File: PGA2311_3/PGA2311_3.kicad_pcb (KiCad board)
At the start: 2 copper layers, 234 x 58 mm, 210 parts, among them J201 3, J202 3, J203 2, J204 2, J205 2, J206 2, J301 Conn_01x16, J302 1, J303 Conn_01x02, J304 4, J305 4, J401 1, J402 3, J403 1, Q301 BC817-40, SW301 SW_Push, SW302 Encoder PEC11R, U201 OPA1678IDR, U202 CD74HCT4052, U203 CD74HCT4052, U204 LM337LM, U205 PGA2311UA, U206 LM317LIDR, U207 UA78L05AIDR, U301 TPS60403DBV, U302 WH1602B, U303 SN74LVC8T245DW, U304 STM32G070KBT6, U305 TLV1117-50IDC, U306 LP2985-33DBV, U307 SN74LVC2G17DBV

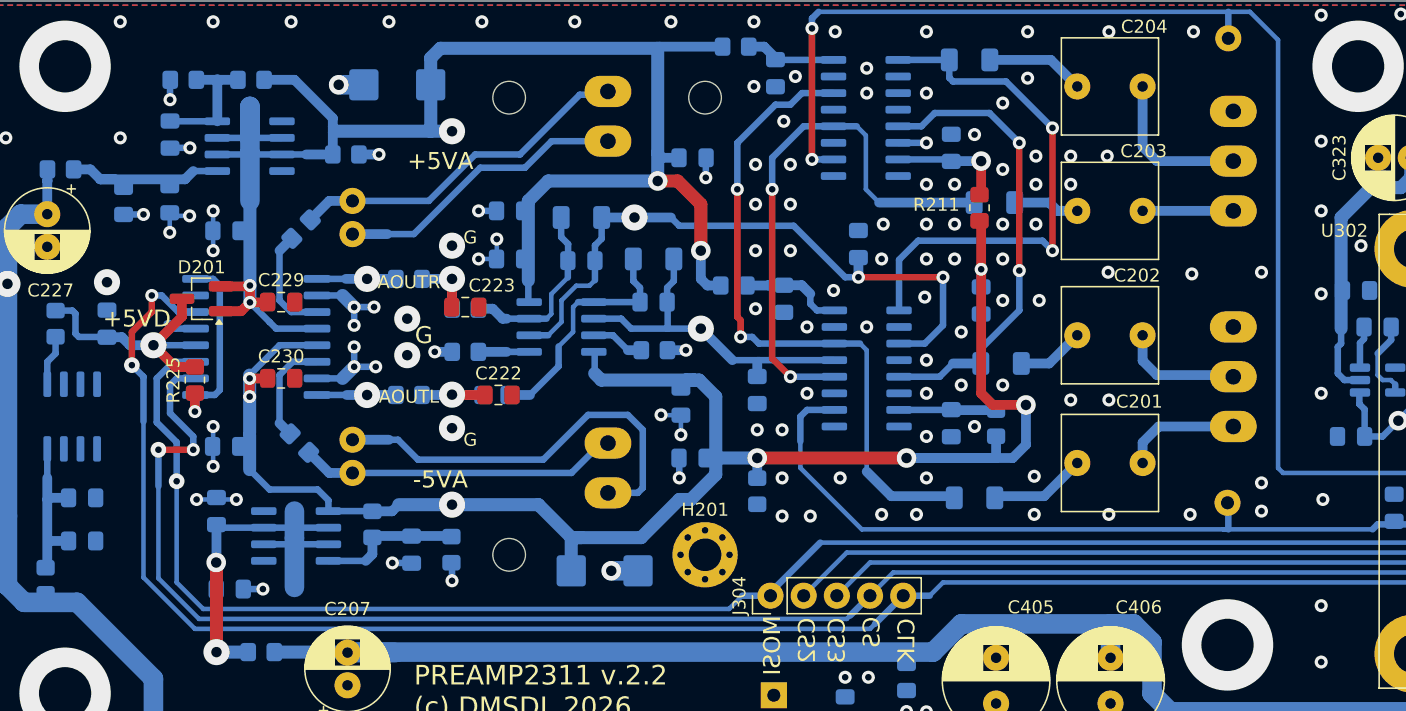
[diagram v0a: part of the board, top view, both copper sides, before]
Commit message: Add files via upload
vias rearranged for connector placement
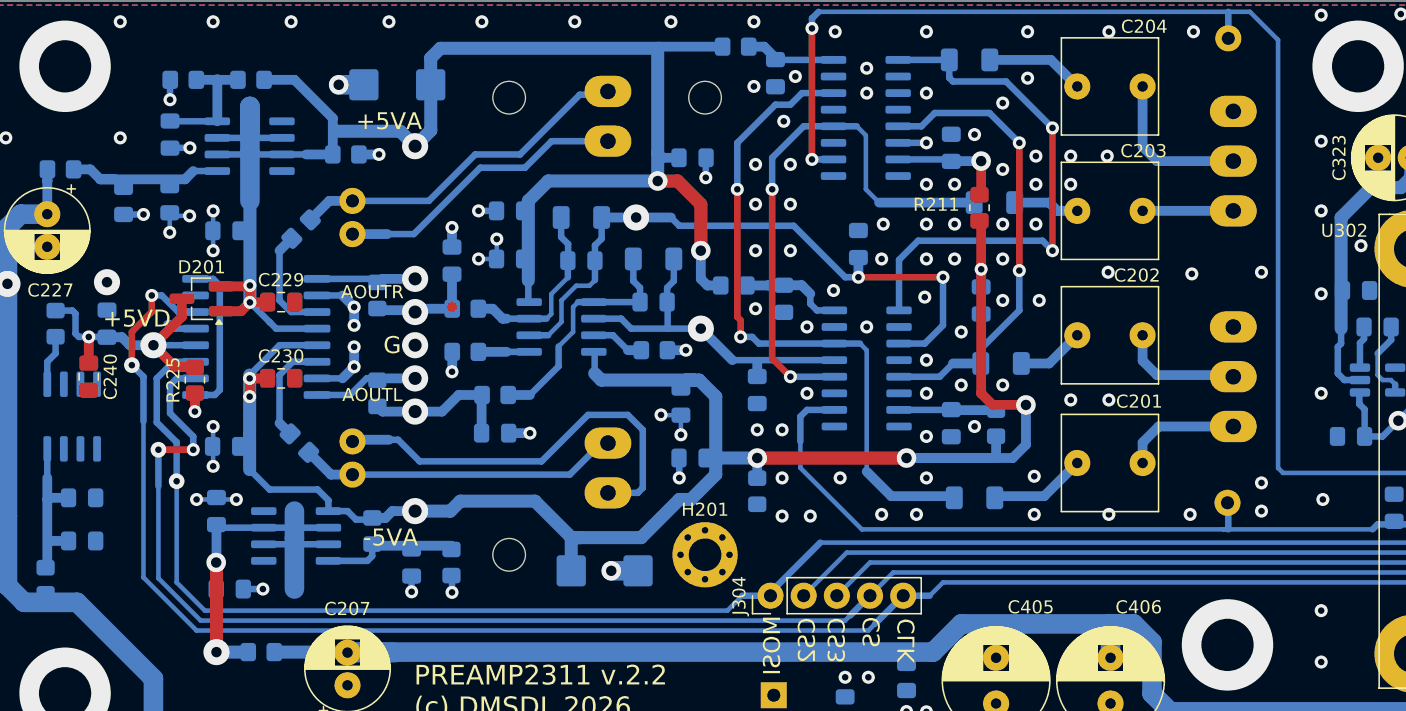
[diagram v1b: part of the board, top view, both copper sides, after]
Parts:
- added C240: 100n, Capacitor_SMD:C_0805_2012Metric_Pad1.18x1.45mm_HandSolder, F.Cu at (27.8, 48.8)
- C222, C223: moved to B.Cu
- moved C223 3.70 mm to (55.6, 39.9), turned to 90 degrees
- moved C222 2.93 mm to (58.9, 53.1)
- moved R223 2.73 mm to (49.9, 42.5), turned to 90 degrees
- moved R222 2.42 mm to (49.9, 50.0), turned to 90 degrees
- moved C218 0.98 mm to (52.5, 63.0)
- moved R217 0.98 mm to (55.6, 63.0)
- moved R216 0.51 mm to (49.5, 60.6)
- moved J205 0.13 mm to (48.0, 56.3)
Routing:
- net Net-(C222-Pad1): track 7.15 -> 11.6 mm
- net Net-(U204-ADJ): track 14.0 -> 10.8 mm
- net Net-(U205-V_{IN}L): track 6.03 -> 8.05 mm
- net /analog/+5VD1: track 21.0 -> 23.0 mm, vias 1 -> 2
- net Net-(C223-Pad1): track 6.76 -> 8.63 mm
- net Net-(U205-V_{IN}R): track 6.03 -> 7.81 mm
- net /analog/-5VA: track 135.8 -> 136.5 mm
- net /analog/+5VA: track 136.3 -> 135.5 mm
- net GND: track 139.5 -> 139.4 mm, vias 244 -> 241
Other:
- board text removed: "AOUT_L"
- board text removed: "AOUT_R"

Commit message: Add files via upload
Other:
- board text added: "PREAMP2311 v.2.3 (c) DMSDL 2026"
- board text removed: "PREAMP2311 v.2.2 (c) DMSDL 2026"
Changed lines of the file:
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@@
 		)
 	)
-	(gr_text "PREAMP2311 v.2.2\n(c) DMSDL 2026\n\n"
+	(gr_text "PREAMP2311 v.2.3\n(c) DMSDL 2026\n\n"
 		(at 52.705 77.343 0)
 		(layer "F.SilkS")
@@
 		)
 	)
-	(gr_text "PREAMP2311 v.2.2\n(c) DMSDL 2026\n\n"
+	(gr_text "PREAMP2311 v.2.3\n(c) DMSDL 2026\n\n"
 		(at 74.041 76.2 0)
 		(layer "B.SilkS")

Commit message: Add files via upload
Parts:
- moved R226 2.45 mm to (27.9, 32.0)
- moved C227 1.27 mm to (24.6, 35.1)
- moved C228 0.25 mm to (30.7, 35.3)
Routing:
- net +9VA: track 323.6 -> 326.5 mm
- net Net-(U206-VI): track 12.7 -> 11.3 mm
- net GND: track 139.4 -> 139.5 mm, vias 241 -> 243
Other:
- board text added: "AOL"
- board text added: "AOR"
- board text added: "PIL"
- board text added: "PIR"

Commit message: Add files via upload
v.2.4 connector to +VA line added
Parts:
- added J207: 2, Connector_PinHeader_2.54mm:PinHeader_1x02_P2.54mm_Vertical, F.Cu at (24.9, 40.5)
- moved R226 1.80 mm to (29.7, 31.8)
- moved C227 1.27 mm to (24.6, 33.8)
- moved C228 0.64 mm to (30.7, 35.9)
- moved C231 0.64 mm to (34.0, 35.8)
- moved C411 0.25 mm to (225.6, 53.6)
- moved C412 0.25 mm to (216.4, 53.6)
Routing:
- net +9VA: track 326.5 -> 328.4 mm, vias 2 -> 1
- net /analog/+5VA: track 135.5 -> 136.5 mm
- net Net-(U206-VI): track 11.3 -> 10.4 mm
- net /mcu/KEY: track 5.90 -> 6.46 mm
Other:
- board text added: "PREAMP2311 v.2.4 (c) DMSDL 2026"
- board text removed: "PREAMP2311 v.2.3 (c) DMSDL 2026"

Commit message: Add files via upload
78l05 output R0 removed
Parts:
- removed R234: 0, Resistor_SMD:R_0805_2012Metric_Pad1.20x1.40mm_HandSolder
- C240: moved to B.Cu
- R205, R206: value 10 -> 100
- moved C240 4.60 mm to (25.7, 44.7), turned to 90 degrees
- moved C213 0.25 mm to (37.6, 59.3)
- moved C221 0.25 mm to (38.3, 53.8)
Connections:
- U207 pad 1: Net-(U207-OUT) -> /analog/+5VD1
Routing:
- net Net-(U207-OUT): track 3.90 -> 0.00 mm
- net /analog/MCU_SCLK: track 132.0 -> 133.1 mm
- net GND: track 139.5 -> 138.5 mm, vias 243 -> 245
- net /analog/+5VD1: track 23.0 -> 23.6 mm, vias 2 -> 1
